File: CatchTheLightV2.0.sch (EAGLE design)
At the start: 37 parts, among them U1 ATMEGA328PB-MUR

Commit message: Update CatchTheLightV2.0.sch
modified Schematic to add features
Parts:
- added S1: SKHMPSE010, switch:SKHMPSE010
- R1: value 220 -> 330
- R2: value 0 -> 330
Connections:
- net N$4 renamed LED_ANODE
- removed net N$1: LED25.C, U1.PE2
- removed net ~RESET/DW: R2.2, R6.1
- new net EPAD: U1.EPAD
- new net PE2: LED9.C, U1.PE2
- new net SPARE_BUTTON_SIGNAL: R2.1, S1.2.1, S1.2.2
- new net ~RESET/DW1: R6.1
- net GND: now also S1.1.1, S1.1.2, S1.SH
- net PB0: now also LED18.C; no longer LED5.C
- net PB1: now also LED19.C; no longer LED4.C
- net PB2: now also LED20.C; no longer LED3.C
- net PB3: now also LED21.C; no longer LED2.C
- net PB4: now also LED22.C; no longer LED1.C
- net PB5: now also LED23.C; no longer LED14.C
- net PB6: now also LED24.C; no longer LED15.C
- net PB7: now also LED25.C; no longer LED16.C
- net PC0: now also LED1.C; no longer LED17.C
- net PC1: now also LED2.C; no longer LED18.C
- net PC2: now also LED3.C; no longer LED19.C
- net PC3: now also LED4.C; no longer LED20.C
- net PC4: now also LED5.C; no longer LED21.C
- net PC5: now also LED6.C; no longer LED22.C
- net PC6: no longer R2.1
- net PD0: now also LED10.C; no longer LED13.C
- net PD1: now also LED11.C; no longer LED12.C
- net PD2: now also LED12.C; no longer LED11.C
- net PD3: now also LED13.C; no longer LED10.C
- net PD4: now also LED14.C; no longer LED9.C
- net PD5: now also LED15.C; no longer LED8.C
- net PD6: now also LED16.C; no longer LED7.C
- net PD7: now also LED17.C; no longer LED6.C
- net PE0: now also LED7.C; no longer LED23.C
- net PE1: now also LED8.C; no longer LED24.C
- net VCC_TARGET: now also R2.2, R6.2
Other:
- note added: "B"
- note added: "Battery"
- note added: "Center LEDs"
- note added: "Current Limiting"
- note added: "Programming Signal Resistors"
- note added: "QTouch Sensor Series Resistor"
- note added: "QTouch/Backup Jumper"
- note added: "RESET LINE PULLUP"
- note added: "Ring LEDs"
- note added: "Spare/Backup Button"
- note removed: "A"
- moved on the sheet: BT1, C1, C2, C3, LED1, LED10, LED11, LED12, LED13, LED14, LED15, LED16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

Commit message: Update CatchTheLightV2.0.sch
Created CustomParts.lbr for backup push button and power switch components, implemented them into schematic.
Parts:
- removed R2: 330, rcl:R-US_R0805
- removed S1: SKHMPSE010, switch:SKHMPSE010
- added B1: (no value), PatternAgents-TouchWidgets:BUTTON_PASSIVE12MM
- added J1: TC2030-IDC-NL, TC2030-IDC-NL:TC2030-IDC-NL
- added R8: 0, rcl:R-US_R0805
- added R9: 100k, rcl:R-US_R0805
- added U$1: SK-3296S-01-L1, CustomParts:SK-3296S-01-L1
- added U$2: TS-1102S-C-A-B, CustomParts:TS-1102S-C-A-B
- R6: value 3.3k -> 100k
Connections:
- removed net PC6: U1.PC6
- new net VCC_BATTERY: BT1.+, U$1.3
- net GND: now also J1.6, U$1.1, U$2.3, U$2.4; no longer S1.1.1, S1.1.2, S1.SH
- net MISO: now also J1.1
- net MOSI: now also J1.4
- net PE3: now also R8.2
- net QTOUCH: now also B1.BUTTON
- net SCK: now also J1.3
- net SPARE_BUTTON_SIGNAL: now also R8.1, R9.1, U$2.1, U$2.2; no longer R2.1, S1.2.1, S1.2.2
- net VCC_TARGET: now also J1.2, R9.2, U$1.2; no longer BT1.+, R2.2
- net ~RESET/DW1: now also J1.5, U1.PC6
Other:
- note added: "6-Pin Plug-Of-Nails Programming Header"
- note added: "C"
- note added: "Michael Bisbano"
- note added: "Power Switch"
- note added: "QTouch Sensor"
- note added: "QTouch/Backup Selection"
- note removed: "B"
- note removed: "QTouch/Backup Jumper"
- moved on the sheet: BT1, C1, C2, C3, LED23, LED24, LED25, R1, R3, R4, R5, R6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

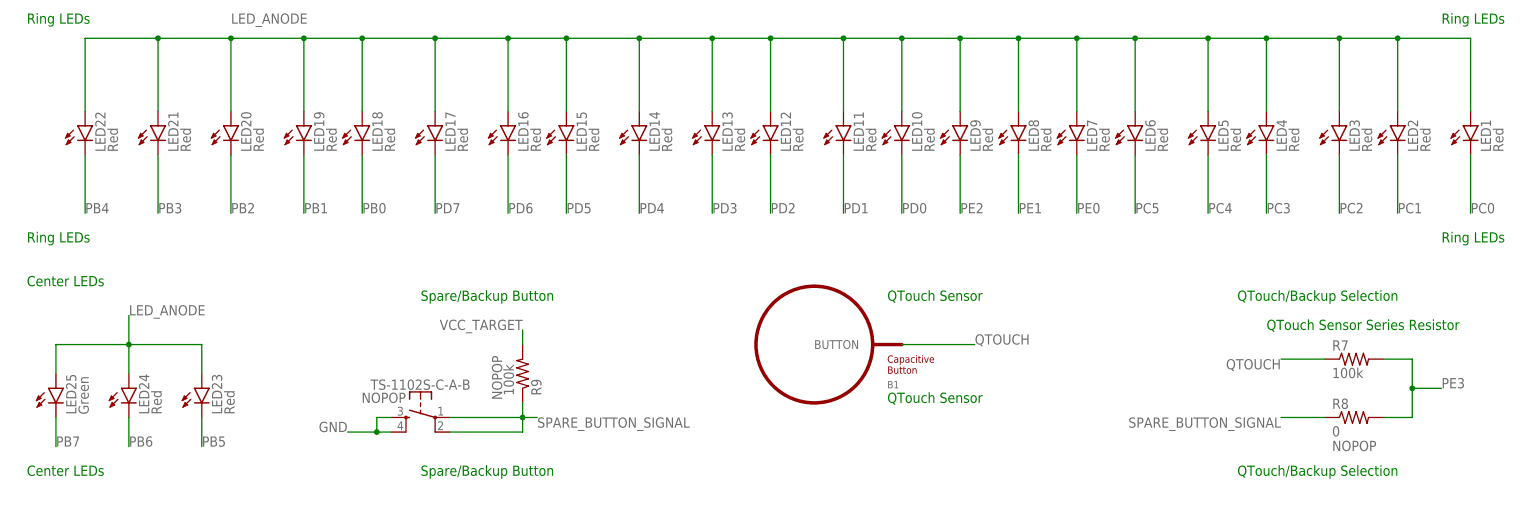
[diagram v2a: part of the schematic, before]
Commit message: Replaced Old Switch and Button components
New Library components added, in process of modifying bom
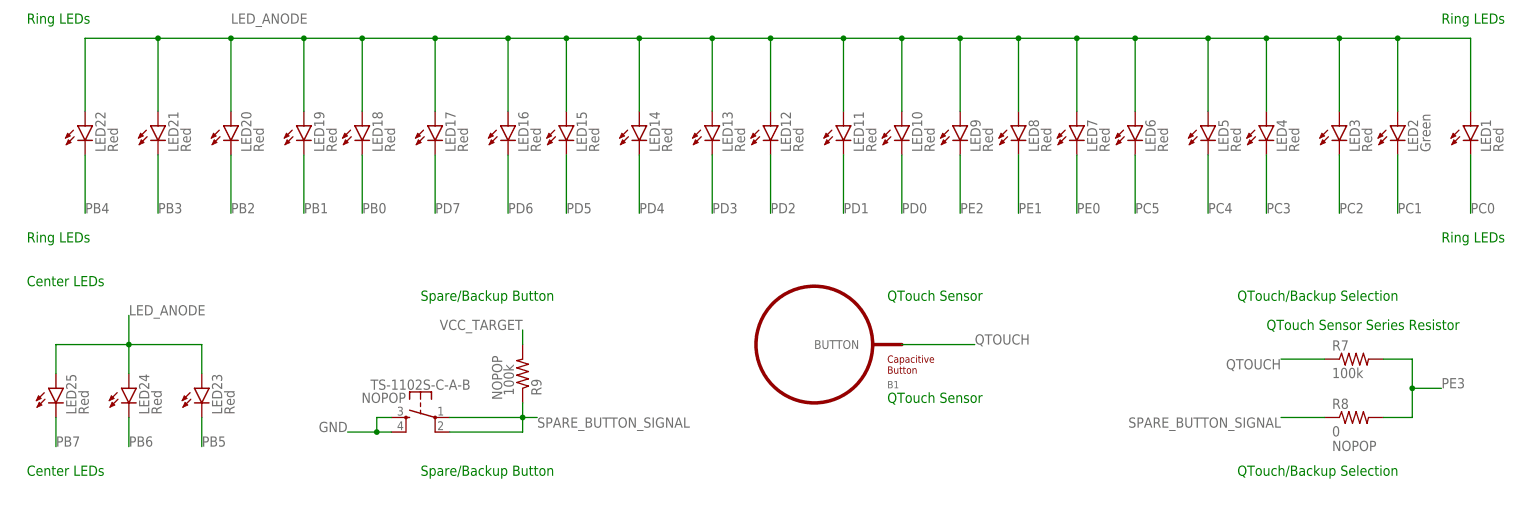
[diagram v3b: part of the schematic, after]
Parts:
- LED2: value Red -> Green
- LED25: value Green -> Red
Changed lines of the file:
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@@
 <part name="LED4" library="led" library_urn="urn:adsk.eagle:library:259" deviceset="LED" device="CHIP-LED0805" package3d_urn="urn:adsk.eagle:package:15818/2" value="Red"/>
 <part name="LED3" library="led" library_urn="urn:adsk.eagle:library:259" deviceset="LED" device="CHIP-LED0805" package3d_urn="urn:adsk.eagle:package:15818/2" value="Red"/>
-<part name="LED2" library="led" library_urn="urn:adsk.eagle:library:259" deviceset="LED" device="CHIP-LED0805" package3d_urn="urn:adsk.eagle:package:15818/2" value="Red"/>
+<part name="LED2" library="led" library_urn="urn:adsk.eagle:library:259" deviceset="LED" device="CHIP-LED0805" package3d_urn="urn:adsk.eagle:package:15818/2" value="Green"/>
 <part name="LED1" library="led" library_urn="urn:adsk.eagle:library:259" deviceset="LED" device="CHIP-LED0805" package3d_urn="urn:adsk.eagle:package:15818/2" value="Red"/>
 <part name="LED23" library="led" library_urn="urn:adsk.eagle:library:259" deviceset="LED" device="CHIP-LED0805" package3d_urn="urn:adsk.eagle:package:15818/2" value="Red"/>
 <part name="LED24" library="led" library_urn="urn:adsk.eagle:library:259" deviceset="LED" device="CHIP-LED0805" package3d_urn="urn:adsk.eagle:package:15818/2" value="Red"/>
-<part name="LED25" library="led" library_urn="urn:adsk.eagle:library:259" deviceset="LED" device="CHIPLED_0805" package3d_urn="urn:adsk.eagle:package:15821/2" value="Green"/>
+<part name="LED25" library="led" library_urn="urn:adsk.eagle:library:259" deviceset="LED" device="CHIPLED_0805" package3d_urn="urn:adsk.eagle:package:15821/2" value="Red"/>
 <part name="B1" library="PatternAgents-TouchWidgets" deviceset="BUTTON_PASSIVE" device="12MM"/>
 <part name="R8" library="rcl" library_urn="urn:adsk.eagle:library:334" deviceset="R-US_" device="R0805" package3d_urn="urn:adsk.eagle:package:23553/2" value="0">

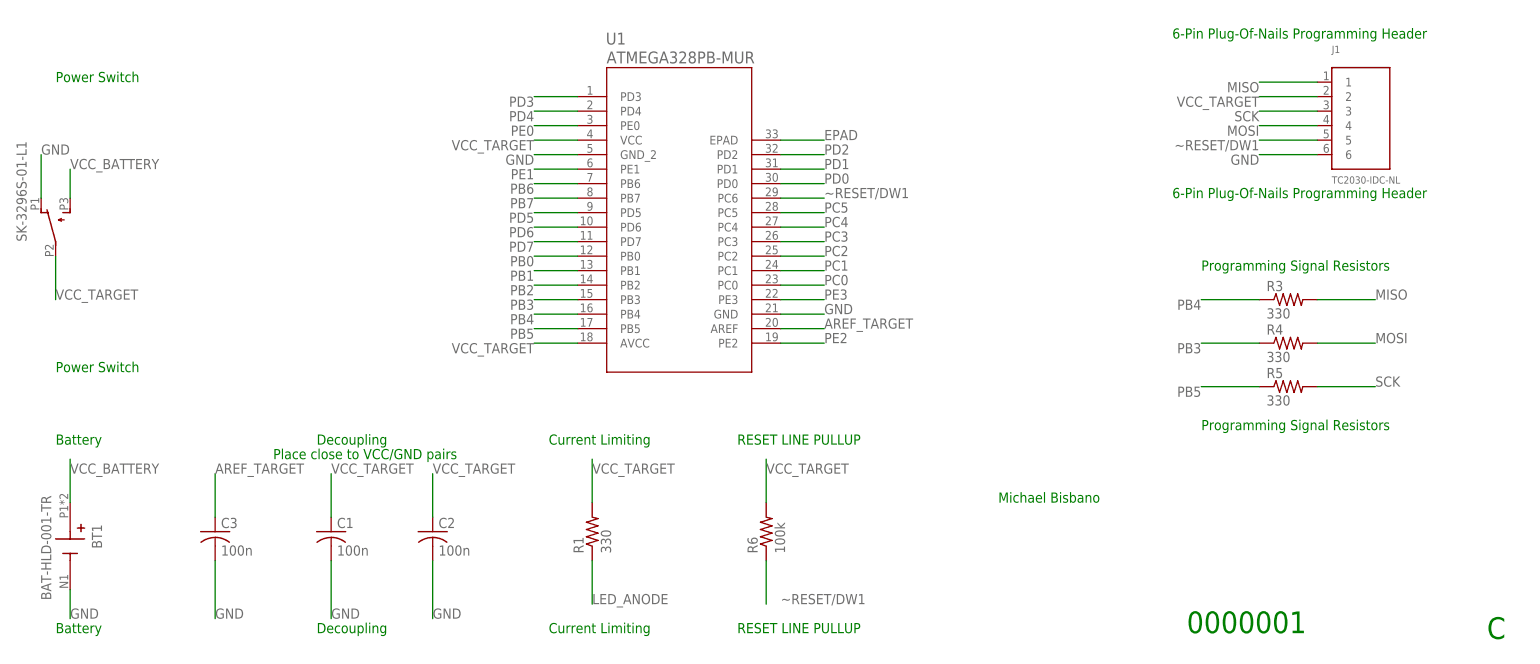
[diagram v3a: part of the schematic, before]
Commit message: Updated Battery Holder
Battery holder updated in schematic, Custom Parts Library, and in BOM. Price not included in BOM for Battery holder as we cannot find it online
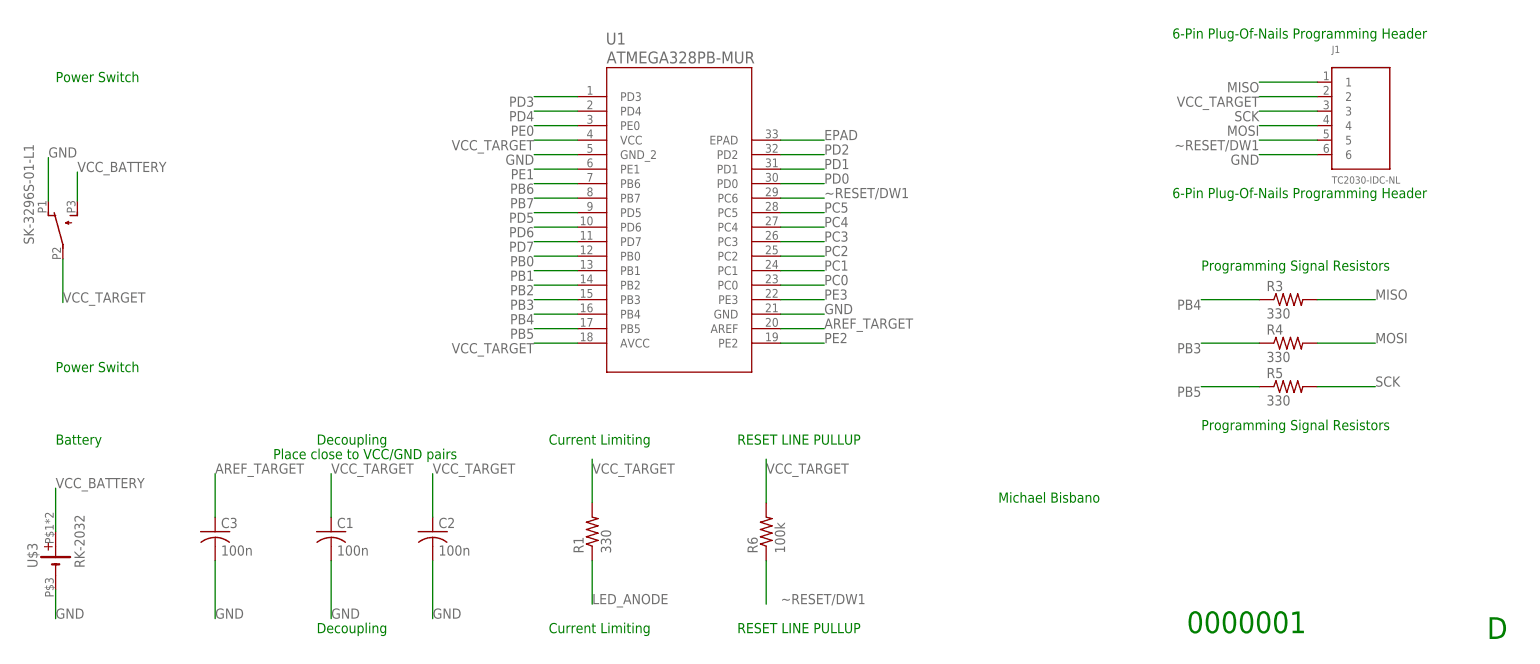
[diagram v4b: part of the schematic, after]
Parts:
- removed BT1: BAT-HLD-001-TR, BAT-HLD-001-TR:BAT-HLD-001-TR
- added U$3: RK-2032, CustomParts:RK-2032
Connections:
- net GND: now also U$3.-; no longer BT1.-
- net VCC_BATTERY: now also U$3.+; no longer BT1.+
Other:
- note added: "D"
- note removed: "C"
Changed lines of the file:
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@@
 <part name="FRAME1" library="frames" library_urn="urn:adsk.eagle:library:229" deviceset="FRAME_A_L" device=""/>
 <part name="R1" library="rcl" library_urn="urn:adsk.eagle:library:334" deviceset="R-US_" device="R0805" package3d_urn="urn:adsk.eagle:package:23553/2" value="330"/>
-<part name="BT1" library="BAT-HLD-001-TR" deviceset="BAT-HLD-001-TR" device=""/>
 <part name="U1" library="328PBMUR" deviceset="ATMEGA328PB-MUR" device=""/>
 <part name="R6" library="rcl" library_urn="urn:adsk.eagle:library:334" deviceset="R-US_" device="R0805" package3d_urn="urn:adsk.eagle:package:23553/2" value="100k"/>
@@
 <attribute name="NOPOP" value="NOPOP"/>
 </part>
+<part name="U$3" library="CustomParts" deviceset="RK-2032" device=""/>
 </parts>
 <sheets>
@@
 <text x="60.96" y="-175.26" size="1.778" layer="91">Decoupling</text>
 <text x="60.96" y="-208.28" size="1.778" layer="91">Decoupling</text>
-<text x="265.938" y="-209.296" size="3.81" layer="91">C</text>
+<text x="265.938" y="-209.296" size="3.81" layer="91">D</text>
 <text x="213.36" y="-208.28" size="3.81" layer="91">0000001</text>
 <text x="101.6" y="-175.26" size="1.778" layer="91">Current Limiting</text>
 <text x="101.6" y="-208.28" size="1.778" layer="91">Current Limiting</text>
 <text x="15.24" y="-175.26" size="1.778" layer="91">Battery</text>
-<text x="15.24" y="-208.28" size="1.778" layer="91">Battery</text>
 <text x="134.62" y="-175.26" size="1.778" layer="91">RESET LINE PULLUP</text>
 <text x="134.62" y="-208.28" size="1.778" layer="91">RESET LINE PULLUP</text>
@@
 <attribute name="VALUE" x="112.522" y="-194.31" size="1.778" layer="96" rot="R90"/>
 </instance>
-<instance part="BT1" gate="G$1" x="17.78" y="-193.04" smashed="yes" rot="R270">
-<attribute name="NAME" x="21.59" y="-189.23" size="1.778" layer="95" rot="R270"/>
-<attribute name="VALUE" x="12.7" y="-184.15" size="1.778" layer="96" rot="R270"/>
-</instance>
 <instance part="U1" gate="A" x="104.14" y="-114.3" smashed="yes">
 <attribute name="NAME" x="111.6076" y="-105.1814" size="2.0828" layer="95" ratio="6" rot="SR0"/>
@@
 <attribute name="VALUE" x="238.7598" y="-129.5404" size="1.27005" layer="96"/>
 </instance>
-<instance part="U$1" gate="G$1" x="15.24" y="-137.16" smashed="yes" rot="R90"/>
+<instance part="U$1" gate="G$1" x="16.51" y="-137.668" smashed="yes" rot="R90"/>
 <instance part="U$2" gate="G$1" x="78.74" y="-81.28" smashed="yes" rot="MR0">
 <attribute name="NOPOP" x="76.2" y="-78.74" size="1.778" layer="96" rot="MR0"/>
@@
 <attribute name="VALUE" x="93.218" y="-77.47" size="1.778" layer="96" rot="MR90"/>
 <attribute name="NOPOP" x="91.186" y="-78.232" size="1.778" layer="96" rot="MR90"/>
+</instance>
+<instance part="U$3" gate="G$1" x="15.24" y="-195.58" smashed="yes" rot="R90">
+<attribute name="NAME" x="12.065" y="-196.85" size="1.778" layer="95" rot="R90"/>
+<attribute name="VALUE" x="20.32" y="-196.85" size="1.778" layer="96" rot="R90"/>
 </instance>
 </instances>
@@
 </segment>
 <segment>
-<pinref part="BT1" gate="G$1" pin="-"/>
-<wire x1="17.78" y1="-200.66" x2="17.78" y2="-205.74" width="0.1524" layer="91"/>
-<label x="17.78" y="-205.74" size="1.778" layer="95"/>
-</segment>
-<segment>
 <pinref part="U1" gate="A" pin="GND"/>
 <wire x1="142.24" y1="-152.4" x2="149.86" y2="-152.4" width="0.1524" layer="91"/>
@@
 <segment>
 <pinref part="U$1" gate="G$1" pin="1"/>
-<wire x1="12.7" y1="-132.08" x2="12.7" y2="-124.46" width="0.1524" layer="91"/>
-<label x="12.7" y="-124.46" size="1.778" layer="95"/>
+<wire x1="13.97" y1="-132.588" x2="13.97" y2="-124.968" width="0.1524" layer="91"/>
+<label x="13.97" y="-124.968" size="1.778" layer="95"/>
 </segment>
 <segment>
@@
 <wire x1="71.12" y1="-83.82" x2="73.66" y2="-83.82" width="0.1524" layer="91"/>
 <junction x="71.12" y="-83.82"/>
+</segment>
+<segment>
+<pinref part="U$3" gate="G$1" pin="-"/>
+<wire x1="15.24" y1="-200.66" x2="15.24" y2="-205.74" width="0.1524" layer="91"/>
+<label x="15.24" y="-205.74" size="1.778" layer="95"/>
 </segment>
 </net>
@@
 <segment>
 <pinref part="U$1" gate="G$1" pin="2"/>
-<wire x1="15.24" y1="-142.24" x2="15.24" y2="-149.86" width="0.1524" layer="91"/>
-<label x="15.24" y="-149.86" size="1.778" layer="95"/>
+<wire x1="16.51" y1="-142.748" x2="16.51" y2="-150.368" width="0.1524" layer="91"/>
+<label x="16.51" y="-150.368" size="1.778" layer="95"/>
 </segment>
 <segment>
@@
 <net name="VCC_BATTERY" class="0">
 <segment>
-<pinref part="BT1" gate="G$1" pin="+"/>
-<wire x1="17.78" y1="-177.8" x2="17.78" y2="-185.42" width="0.1524" layer="91"/>
-<label x="17.78" y="-180.34" size="1.778" layer="95"/>
-</segment>
-<segment>
 <pinref part="U$1" gate="G$1" pin="3"/>
-<wire x1="17.78" y1="-132.08" x2="17.78" y2="-127" width="0.1524" layer="91"/>
-<label x="17.78" y="-127" size="1.778" layer="95"/>
-</segment>
-</net>
+<wire x1="19.05" y1="-132.588" x2="19.05" y2="-127.508" width="0.1524" layer="91"/>
+<label x="19.05" y="-127.508" size="1.778" layer="95"/>
+</segment>
+<segment>
+<pinref part="U$3" gate="G$1" pin="+"/>
+<wire x1="15.24" y1="-190.5" x2="15.24" y2="-182.88" width="0.1524" layer="91"/>
+<label x="15.24" y="-182.88" size="1.778" layer="95"/>
+</segment>
+</net>
